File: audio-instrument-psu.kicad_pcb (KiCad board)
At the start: 2 copper layers, 100 x 50 mm, 45 parts, among them J1 Molex_SL_01x04_Male, J2 Molex_SL_01x04_Male, J3 Molex_SL_01x04_Male, J4 Molex_SL_01x04_Male, J5 Molex_SL_01x04_Male, U1 LM317_TO-220, U2 LM337_TO220

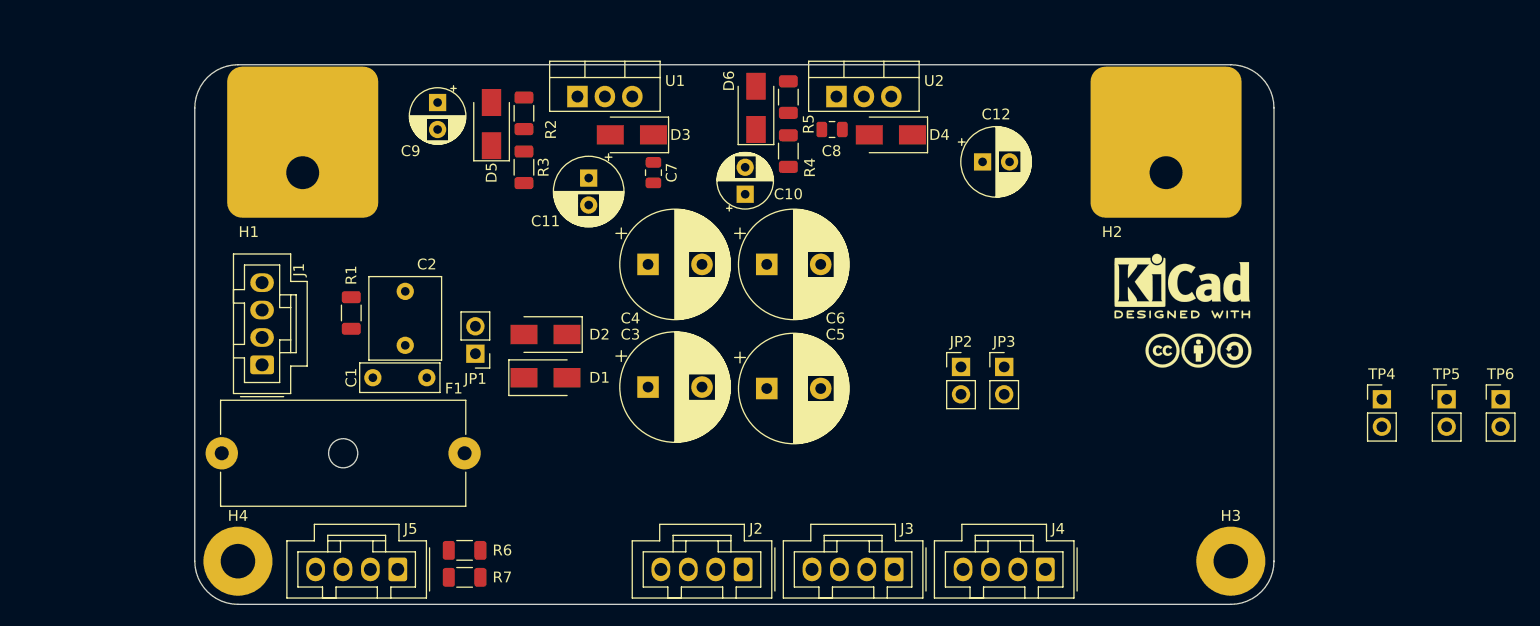
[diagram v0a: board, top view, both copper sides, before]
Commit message: initial routing complete, DRC clean
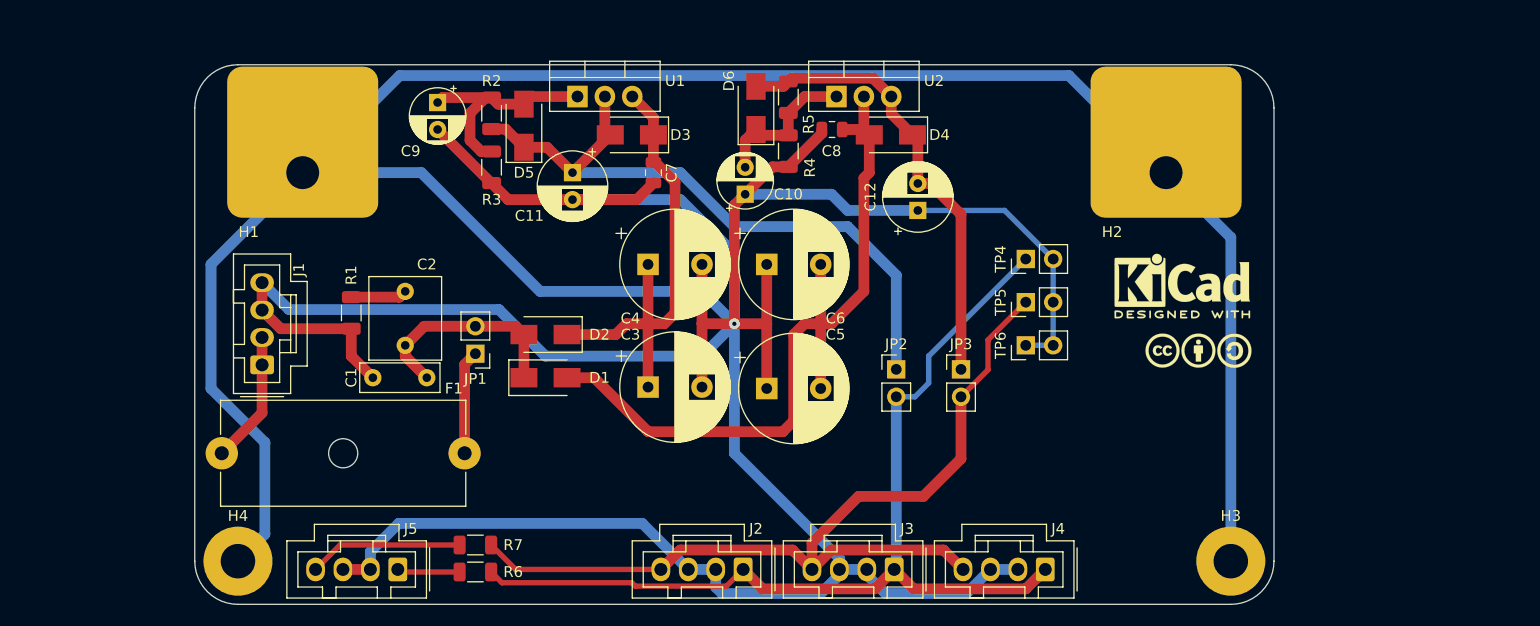
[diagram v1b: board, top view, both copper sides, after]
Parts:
- moved TP6 44.3 mm to (167.0, 100.0), turned to 90 degrees
- moved TP5 40.0 mm to (167.0, 96.0), turned to 90 degrees
- moved TP4 35.5 mm to (167.0, 92.0), turned to 90 degrees
- moved C12 7.50 mm to (157.0, 87.5), turned to 90 degrees
- moved JP2 6.00 mm to (155.0, 102.2)
- moved JP3 4.01 mm to (161.0, 102.2)
- moved R7 3.16 mm to (116.0, 118.5), turned to 180 degrees
- moved D5 3.00 mm to (120.5, 79.7)
- moved R2 3.00 mm to (117.5, 78.5)
- moved R3 3.00 mm to (117.5, 83.5)
- moved R6 2.24 mm to (116.0, 121.0), turned to 180 degrees
- moved C11 1.58 mm to (125.0, 84.0)
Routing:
- net GND: track 0.00 -> 517.7 mm, vias 0 -> 1
- net +12V: track 0.00 -> 90.3 mm
- net -12V: track 0.00 -> 84.1 mm
- net /-12V_regin: track 0.00 -> 71.6 mm
- net /+12V_regout: track 0.00 -> 60.5 mm
- net /+12V_regin: track 0.00 -> 44.0 mm
- net /-12V_regout: track 0.00 -> 42.2 mm
- net Net-(C9-Pad1): track 0.00 -> 21.2 mm
- net /12VAC_fused: track 0.00 -> 19.9 mm
- net Net-(C10-Pad2): track 0.00 -> 14.3 mm
- net Net-(J5-Pad4): track 0.00 -> 14.3 mm
- net /12VAC_unfused: track 0.00 -> 12.3 mm
- net Net-(F1-Pad1): track 0.00 -> 9.64 mm
- net Net-(J5-Pad1): track 0.00 -> 5.82 mm
- net Net-(C2-Pad2): track 0.00 -> 5.22 mm
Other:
- board text added: "TODO - move mounting brackets outwards to where heatsink will mount to case? - label jumpers, testpoints, and connectors"
- board text removed: "TODO - move mounting brackets outwards to where heatsink will mount to case?"

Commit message: change board to attach to heatsink mounting holes
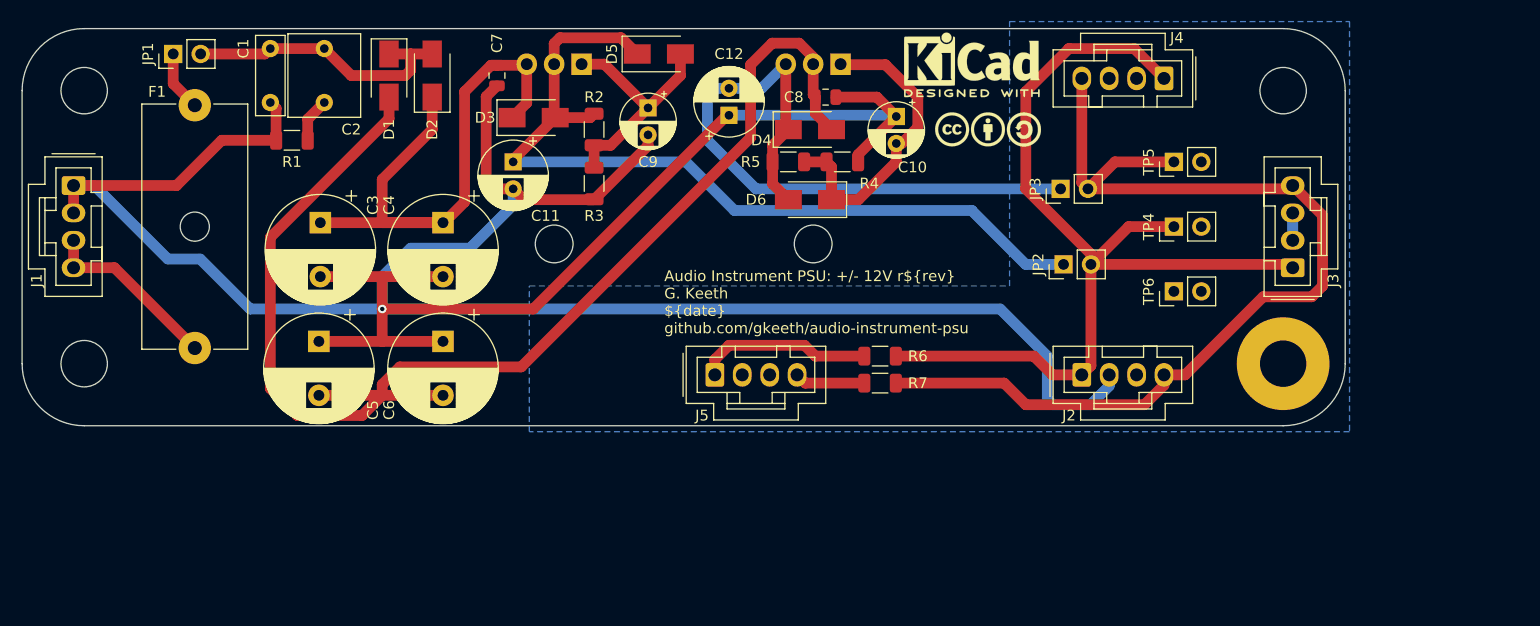
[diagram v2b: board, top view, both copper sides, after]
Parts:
- H1, H2: value MountingHole_Pad -> MountingHole; footprint Mounting_gkeeth:MountingBracket_Keystone_4335_Width12.7mm_Drill3.05mm -> MountingHole:MountingHole_4.3mm_M4
- H3: footprint MountingHole:MountingHole_3.2mm_M3_Pad -> MountingHole:MountingHole_4.3mm_M4_Pad
- H4: value MountingHole_Pad -> MountingHole; footprint MountingHole:MountingHole_3.2mm_M3_Pad -> MountingHole:MountingHole_4.3mm_M4
- U1, U2: footprint Package_TO_SOT_THT:TO-220-3_Vertical -> Package_TO_SOT_THT:TO-220-3_Horizontal_TabUp; moved to B.Cu
- moved J4 46.8 mm to (179.8, 75.3)
- moved J3 46.3 mm to (191.7, 92.8), turned to 90 degrees
- moved R6 42.5 mm to (153.5, 101.0)
- moved C5 41.7 mm to (101.5, 99.6), turned to -90 degrees
- moved F1 40.8 mm to (90.0, 77.8), turned to -90 degrees
- moved R7 40.4 mm to (153.5, 103.5)
- moved JP1 39.4 mm to (88.0, 73.0), turned to 90 degrees
- moved J2 36.2 mm to (172.2, 102.7), turned to 0 degrees
- moved J5 34.5 mm to (138.2, 102.7), turned to 0 degrees
- moved C3 34.0 mm to (101.6, 88.6), turned to -90 degrees
- moved C1 33.8 mm to (97.0, 72.5), turned to -90 degrees
- moved D2 31.5 mm to (108.0, 75.0), turned to -90 degrees
- moved C6 30.8 mm to (113.0, 99.6), turned to -90 degrees
- moved C2 28.5 mm to (102.0, 72.5), turned to -90 degrees
- moved LOGO1 28.3 mm to (163.5, 80.0)
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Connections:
- J1 pad 1: /12VAC_unfused -> GND
- J1 pad 2: /12VAC_unfused -> GND
- J1 pad 3: GND -> /12VAC_unfused
- J1 pad 4: GND -> /12VAC_unfused
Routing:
- net GND: track 517.7 -> 281.1 mm
- net /-12V_regin: track 71.6 -> 121.2 mm
- net /+12V_regout: track 60.5 -> 79.8 mm
- net /-12V_regout: track 42.2 -> 61.0 mm
- net Net-(C10-Pad2): track 14.3 -> 28.8 mm
- net /+12V_regin: track 44.0 -> 55.9 mm
- net Net-(J5-Pad1): track 5.82 -> 16.2 mm
- net -12V: track 84.1 -> 94.5 mm
- net Net-(J5-Pad4): track 14.3 -> 6.54 mm
- net /12VAC_fused: track 19.9 -> 26.4 mm
- net /12VAC_unfused: track 12.3 -> 16.9 mm
- net Net-(F1-Pad1): track 9.64 -> 5.58 mm
- net Net-(C9-Pad1): track 21.2 -> 22.6 mm
- net Net-(C2-Pad2): track 5.22 -> 4.14 mm
- added copper zone on B.Cu, net GND
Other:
- board size 100 x 50 mm -> 122.6 x 36.8 mm
- board text added: "Audio Instrument PSU: +/- 12V r${rev} G. Keeth ${date} github.com/gkeeth/audio-instrument-psu"
- board text added: "TODO - label jumpers, testpoints, and connectors"
- board text removed: "Audio Instrument PSU: +/- 12V G. Keeth r${rev} ${date} github.com/gkeeth/audio-instrument-psu"
- board text removed: "TODO - move mounting brackets outwards to where heatsink will mount to case? - label jumpers, testpoints, and connectors"

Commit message: redo layout to mount onto heatsink directly
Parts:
- added kibuzzard-6340BBAD: G***, kibuzzard-6340BBAD, F.Cu at (176.0, 79.2)
- added kibuzzard-6340BBAD: G***, kibuzzard-6340BBAD, F.Cu at (176.0, 98.8)
- added kibuzzard-6340BBAD: G***, kibuzzard-6340BBAD, F.Cu at (142.0, 98.8)
- added kibuzzard-6340BBAD: G***, kibuzzard-6340BBAD, F.Cu at (187.8, 89.0)
- added kibuzzard-6340BC06: G***, kibuzzard-6340BC06, F.Cu at (191.8, 80.5)
- added kibuzzard-6340BC0E: G***, kibuzzard-6340BC0E, F.Cu at (165.2, 75.2)
- added kibuzzard-6340BC16: G***, kibuzzard-6340BC16, F.Cu at (165.0, 102.8)
- added kibuzzard-6340BF5D: G***, kibuzzard-6340BF5D, F.Cu at (131.8, 102.8)
- added kibuzzard-6340BF7A: G***, kibuzzard-6340BF7A, F.Cu at (79.5, 97.5)
- added kibuzzard-6340BF8B: G***, kibuzzard-6340BF8B, F.Cu at (83.2, 89.0)
- added kibuzzard-6340BFBC: G***, kibuzzard-6340BFBC, F.Cu at (177.0, 89.0)
- moved LOGO1 77.6 mm to (90.0, 104.8)
- moved LOGO2 47.2 mm to (122.8, 100.2), turned to 90 degrees
- moved TP4 6.13 mm to (182.0, 95.0)
- moved TP6 6.13 mm to (182.0, 89.0)
- moved JP2 2.25 mm to (168.2, 92.5)
- moved JP3 1.97 mm to (168.2, 85.5)
- moved TP5 1.25 mm to (182.0, 83.0)
- moved R6 0.50 mm to (153.5, 100.5)
- moved R7 0.50 mm to (153.5, 103.0)
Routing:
- net +12V: track 90.6 -> 98.3 mm
- net -12V: track 94.5 -> 101.0 mm
- net /+12V_regout: track 79.8 -> 77.6 mm
- net /-12V_regout: track 61.0 -> 59.0 mm
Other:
- board text added: "Audio Instrument PSU r${rev} G. Keeth ${date} github.com/gkeeth/audio-instrument-psu"
- board text removed: "Audio Instrument PSU: +/- 12V r${rev} G. Keeth ${date} github.com/gkeeth/audio-instrument-psu"
- board text removed: "TODO - label jumpers, testpoints, and connectors"
